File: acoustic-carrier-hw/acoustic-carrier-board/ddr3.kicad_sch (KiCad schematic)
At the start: 27 parts, among them IC1101 MT41K256M16TW-107_P

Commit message: [carrier] Added decoupling to LPDDR3 and routed VREF (next) finalize power supply
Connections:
- net VDDR_CORE renamed VLPDDR3_CORE
- net VDDR_DQ renamed VLPDDR3_DQ
- net VLPDRR3_V675 renamed VLPDDR3_V675
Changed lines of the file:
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@@
 	(wire
 		(pts
-			(xy 234.95 33.02) (xy 224.79 33.02)
+			(xy 237.49 33.02) (xy 224.79 33.02)
 		)
 		(stroke
@@
 	(wire
 		(pts
-			(xy 208.28 33.02) (xy 196.85 33.02)
+			(xy 212.09 33.02) (xy 196.85 33.02)
 		)
 		(stroke
@@
 		)
 	)
-	(label "VDDR_CORE"
-		(at 208.28 33.02 180)
-		(effects
-			(font
-				(size 1.27 1.27)
-			)
-			(justify right bottom)
-		)
-	)
 	(label "DDR3.LDM"
 		(at 180.34 82.55 180)
@@
 		)
 	)
+	(label "VLPDDR3_DQ"
+		(at 237.49 33.02 180)
+		(effects
+			(font
+				(size 1.27 1.27)
+			)
+			(justify right bottom)
+		)
+	)
 	(label "DDR3.CS#"
 		(at 261.62 93.98 0)
@@
 		)
 	)
-	(label "VDDR_DQ"
-		(at 57.15 99.06 0)
+	(label "VLPDDR3_DQ"
+		(at 43.18 99.06 0)
 		(effects
 			(font
@@
 		)
 	)
-	(label "VDDR_DQ"
-		(at 234.95 33.02 180)
-		(effects
-			(font
-				(size 1.27 1.27)
-			)
-			(justify right bottom)
-		)
-	)
 	(label "DDR3.DQ4"
 		(at 180.34 97.79 180)
@@
 		)
 	)
-	(label "VDDR_CORE"
+	(label "VLPDDR3_CORE"
 		(at 41.91 55.88 0)
 		(effects
@@
 			)
 			(justify left bottom)
+		)
+	)
+	(label "VLPDDR3_CORE"
+		(at 212.09 33.02 180)
+		(effects
+			(font
+				(size 1.27 1.27)
+			)
+			(justify right bottom)
 		)
 	)
@@
 		)
 	)
-	(global_label "VLPDRR3_V675"
+	(global_label "VLPDDR3_V675"
 		(shape passive)
 		(at 33.02 125.73 0)
@@
 		)
 	)
-	(global_label "VLPDRR3_V675"
+	(global_label "VLPDDR3_V675"
 		(shape passive)
 		(at 181.61 115.57 180)

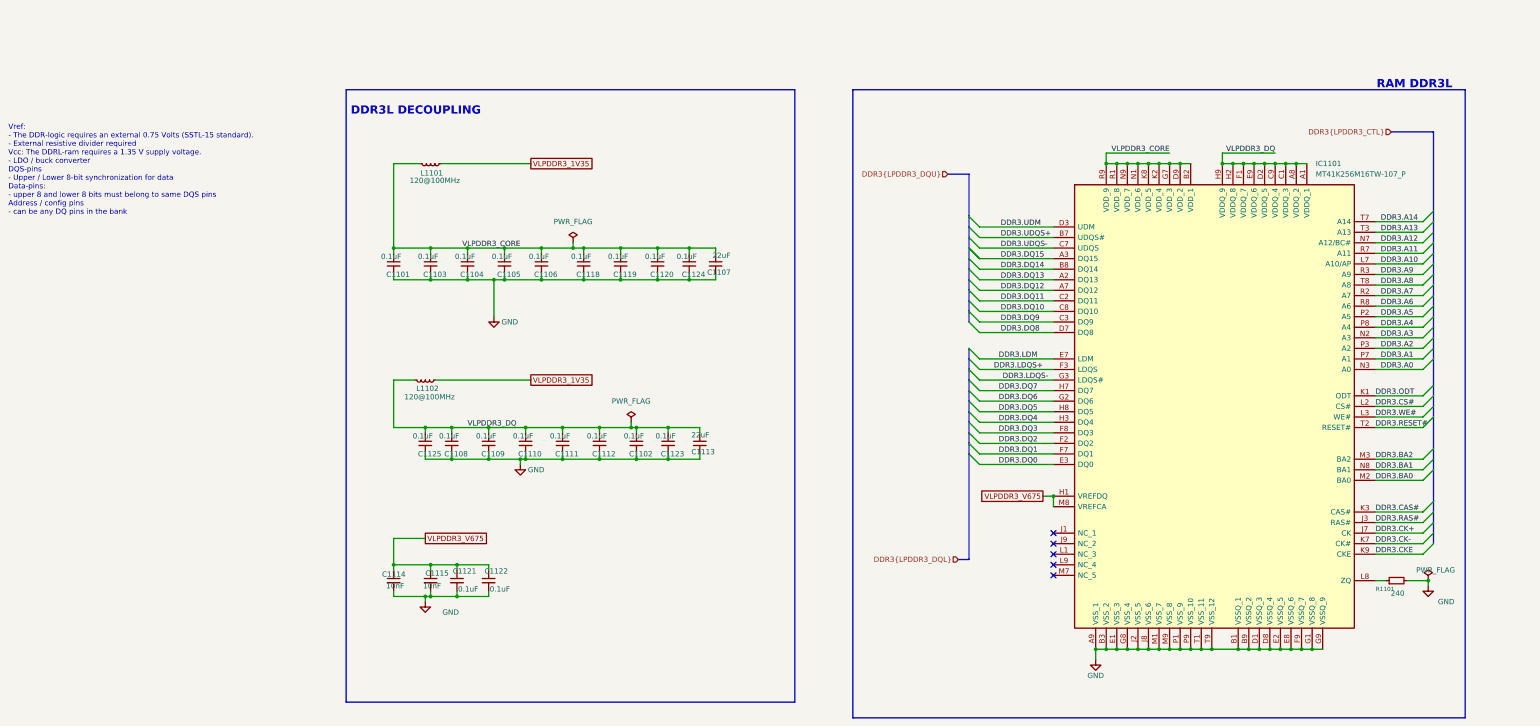
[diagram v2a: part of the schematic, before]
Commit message: [carrier] Further routing, ground plane removal underneath connectors, ..
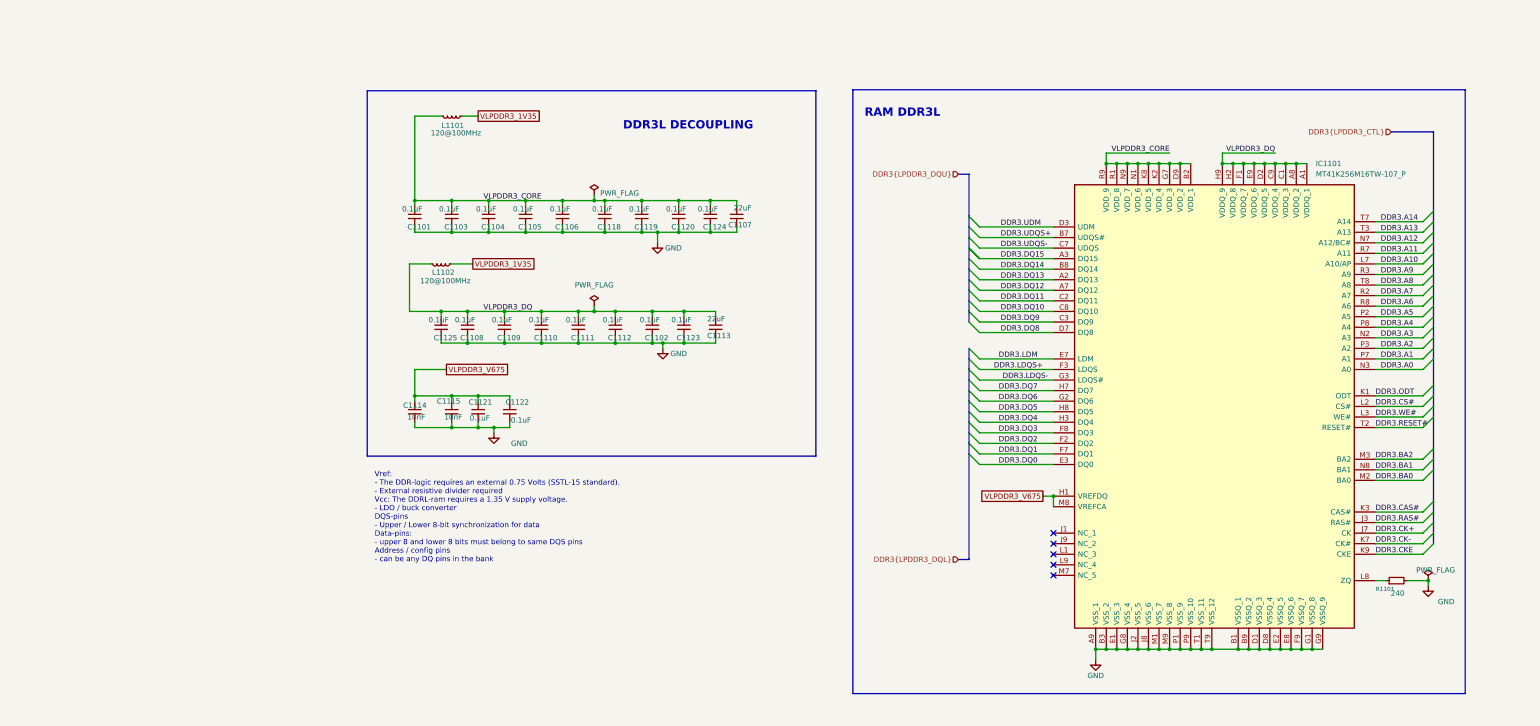
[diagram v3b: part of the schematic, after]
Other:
- moved on the sheet: C1101, C1102, C1103, C1104, C1105, C1106, C1107, C1108, C1109, C1110, C1111, C1112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

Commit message: [carrier] todo: recalculate validity window
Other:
- note added: "RAM LPDDR3"
- note removed: "RAM DDR3L"
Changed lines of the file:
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@@
 		)
 	)
-	(text "RAM DDR3L"
+	(text "RAM LPDDR3"
 		(exclude_from_sim no)
 		(at 147.828 23.368 0)

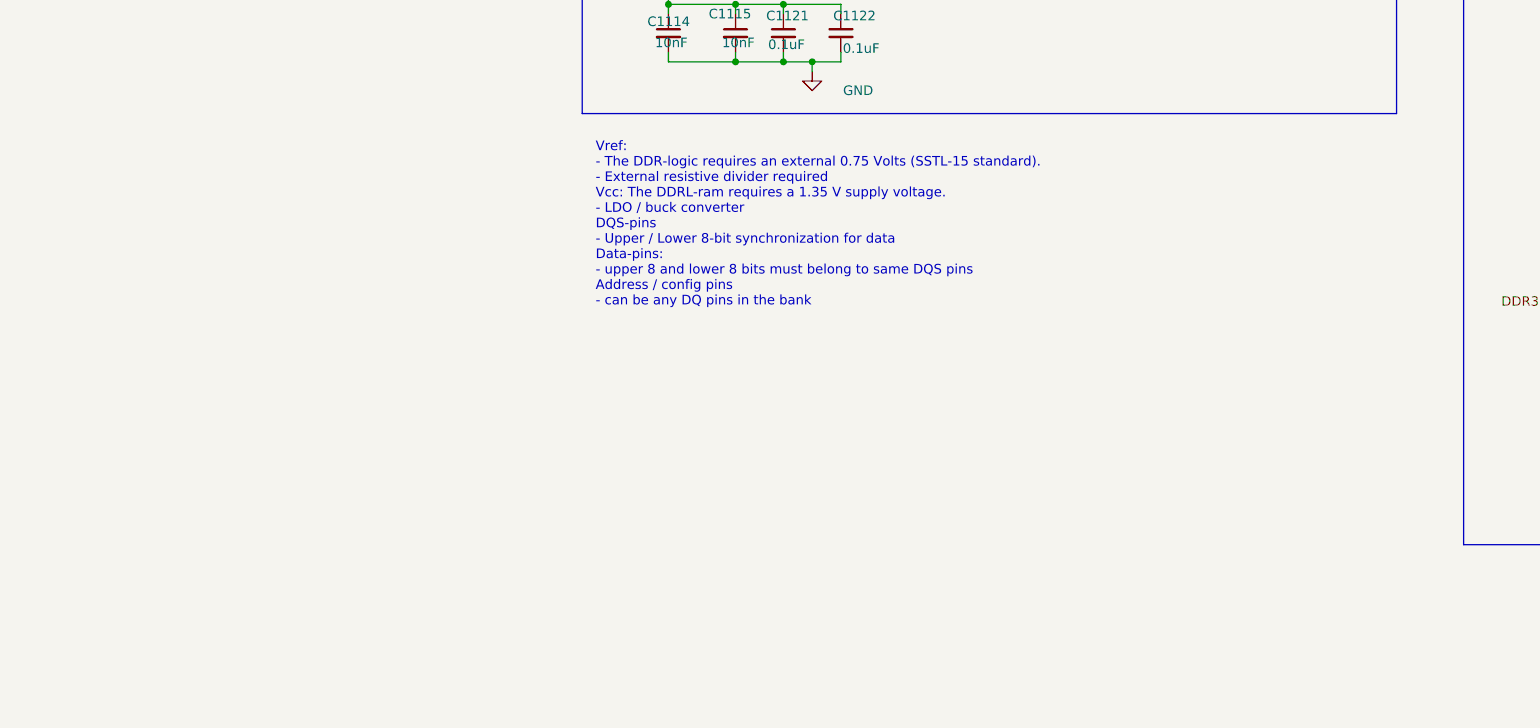
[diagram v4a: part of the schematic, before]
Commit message: [carrier] Added testpoints to lpddr3 (next) do final checks before ordering
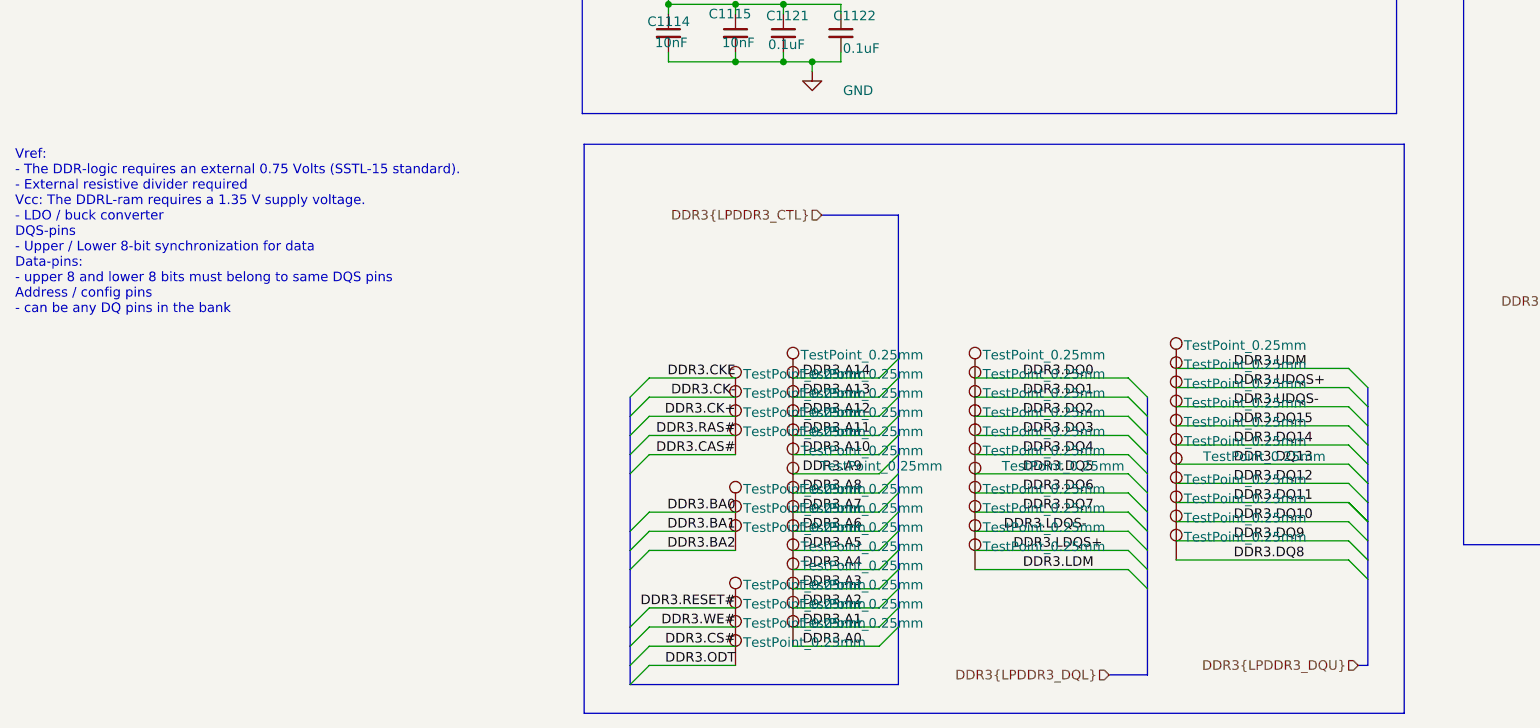
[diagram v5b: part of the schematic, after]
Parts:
- added TP1101, TP1102, TP1103, TP1104, TP1105, TP1106, TP1107, TP1108, TP1109, TP1110, TP1111, TP1112, TP1113, TP1114, TP1115, TP1116, TP1117, TP1118, TP1119, TP1120, TP1121, TP1122, TP1123, TP1124, TP1125, TP1126, TP1127, TP1128, TP1129, TP1130, TP1131, TP1132, TP1133, TP1134, TP1135, TP1136, TP1137, TP1138, TP1139, TP1140, TP1141, TP1142, TP1143, TP1144, TP1145, TP1146, TP1147, TP1148: TestPoint_0.25mm, iw-misc:TestPoint_Pad_D0.25mm, symbol iw-misc:TestPoint_0.25mm
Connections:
- net DDR3.A0: now also TP1137.1
- net DDR3.A1: now also TP1136.1
- net DDR3.A10: now also TP1127.1
- net DDR3.A11: now also TP1126.1
- net DDR3.A12: now also TP1125.1
- net DDR3.A13: now also TP1102.1
- net DDR3.A14: now also TP1101.1
- net DDR3.A2: now also TP1135.1
- net DDR3.A3: now also TP1134.1
- net DDR3.A4: now also TP1133.1
- net DDR3.A5: now also TP1132.1
- net DDR3.A6: now also TP1131.1
- net DDR3.A7: now also TP1130.1
- net DDR3.A8: now also TP1129.1
- net DDR3.A9: now also TP1128.1
- net DDR3.BA0: now also TP1146.1
- net DDR3.BA1: now also TP1147.1
- net DDR3.BA2: now also TP1148.1
- net DDR3.CAS#: now also TP1145.1
- net DDR3.CK+: now also TP1143.1
- net DDR3.CK-: now also TP1142.1
- net DDR3.CS#: now also TP1140.1
- net DDR3.DQ0: now also TP1103.1
- net DDR3.DQ1: now also TP1106.1
- net DDR3.DQ10: now also TP1112.1
- net DDR3.DQ11: now also TP1111.1
- net DDR3.DQ12: now also TP1110.1
- net DDR3.DQ13: now also TP1115.1
- net DDR3.DQ14: now also TP1109.1
- net DDR3.DQ15: now also TP1108.1
- net DDR3.DQ2: now also TP1116.1
- net DDR3.DQ3: now also TP1117.1
- net DDR3.DQ4: now also TP1118.1
- net DDR3.DQ5: now also TP1119.1
- net DDR3.DQ6: now also TP1120.1
- net DDR3.DQ7: now also TP1121.1
- net DDR3.DQ8: now also TP1114.1
- net DDR3.DQ9: now also TP1113.1
- net DDR3.LDM: now also TP1124.1
- net DDR3.LDQS+: now also TP1123.1
- net DDR3.LDQS-: now also TP1122.1
- net DDR3.ODT: now also TP1141.1
- net DDR3.RAS#: now also TP1144.1
- net DDR3.RESET#: now also TP1138.1
- net DDR3.UDM: now also TP1104.1
- net DDR3.UDQS+: now also TP1105.1
- net DDR3.UDQS-: now also TP1107.1
- net DDR3.WE#: now also TP1139.1

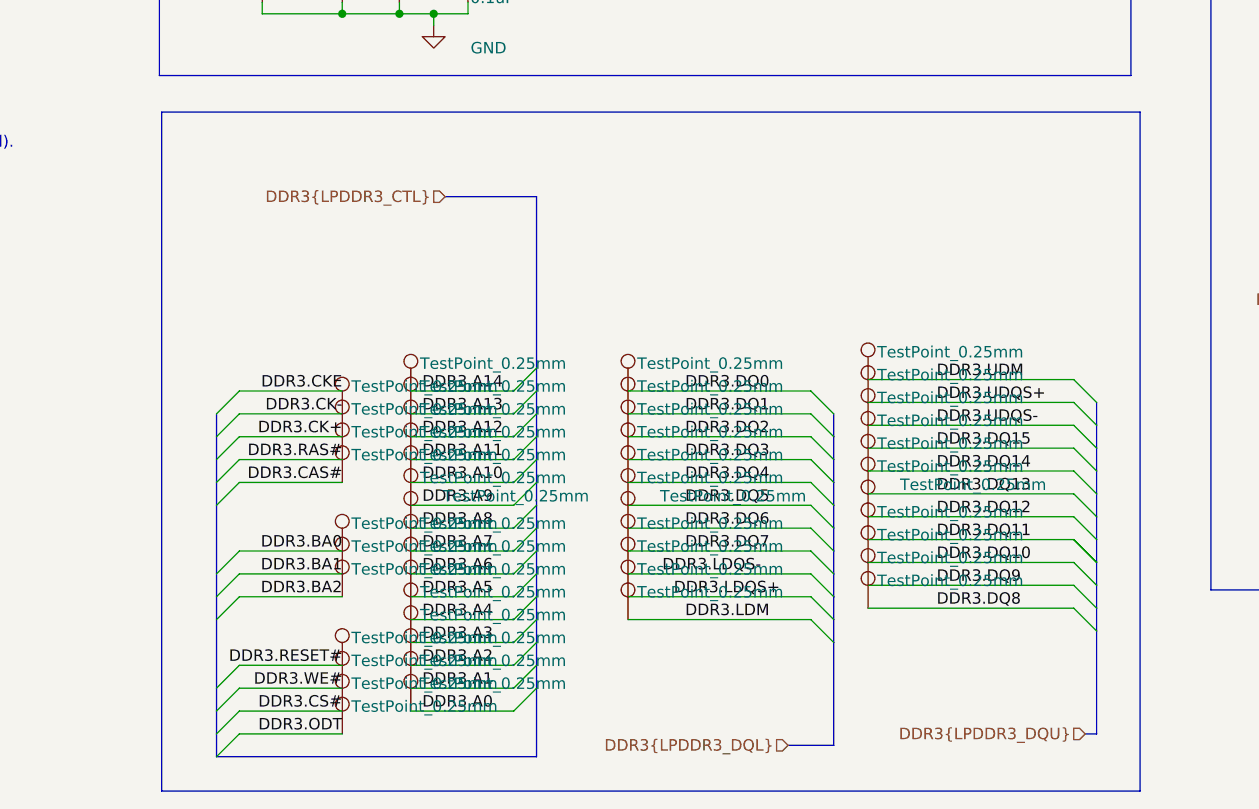
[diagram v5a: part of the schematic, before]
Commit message: [carrier] finished for production (next) reroute the LPDDR3, with appropriate CMD-CTRL bus delays, and change banks for command-control
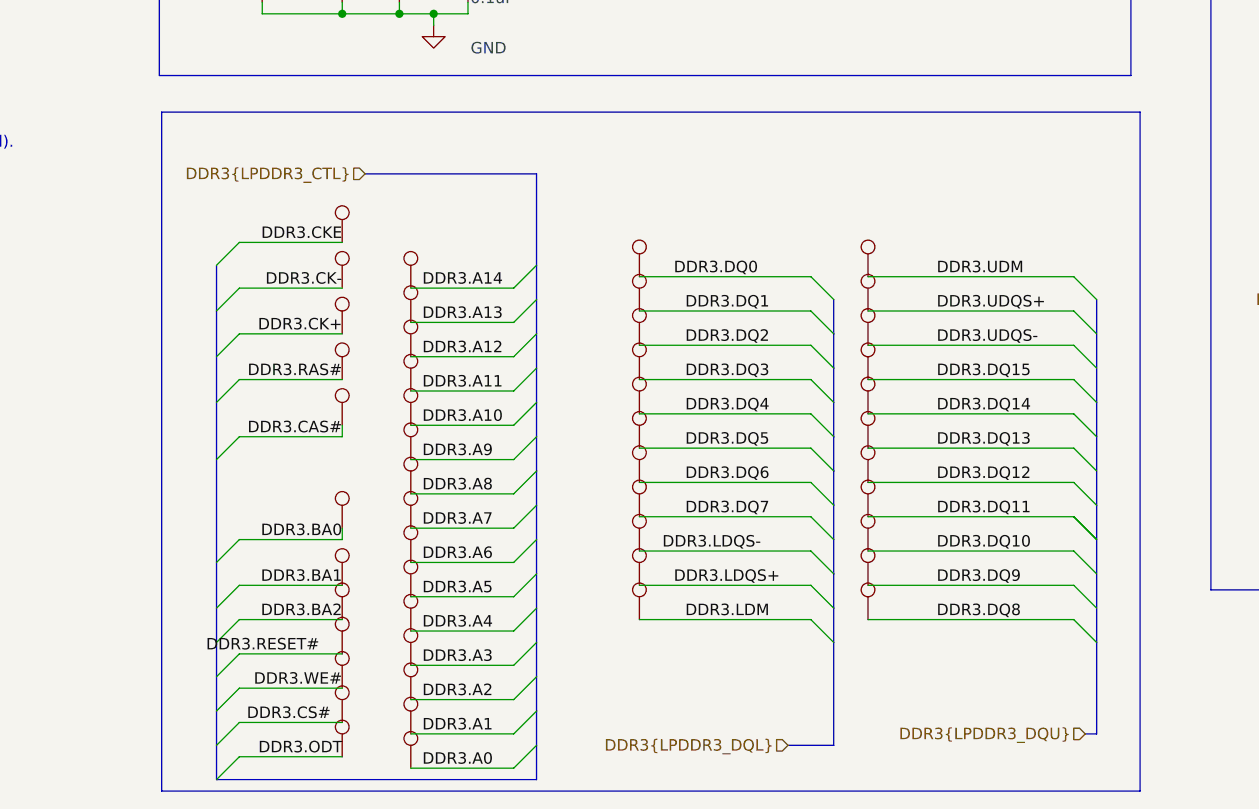
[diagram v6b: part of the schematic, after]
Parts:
- added TP1149: TestPoint_0.25mm, iw-misc:TestPoint_Pad_D0.25mm, symbol iw-misc:TestPoint_0.25mm
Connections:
- net DDR3.CKE: now also TP1149.1

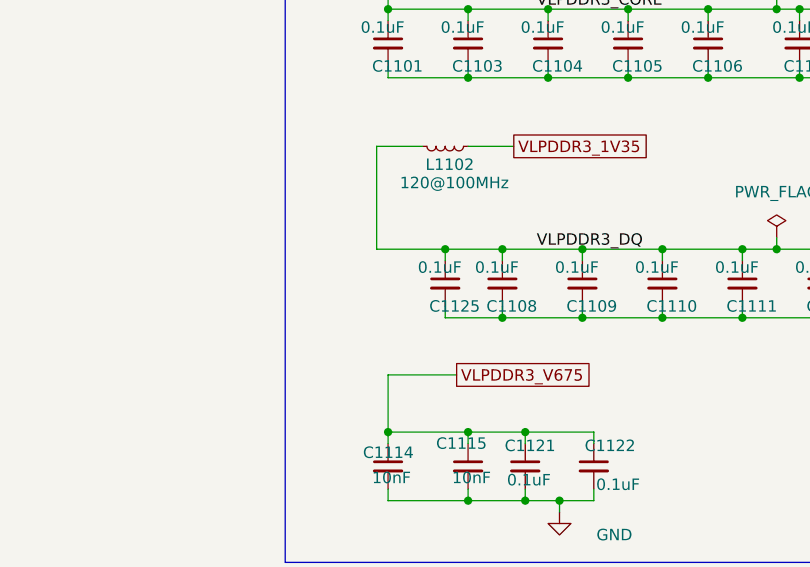
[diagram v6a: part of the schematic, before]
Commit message: [carrier] Finished routing, layed out lpddr3 capacitors (next) route power on plane
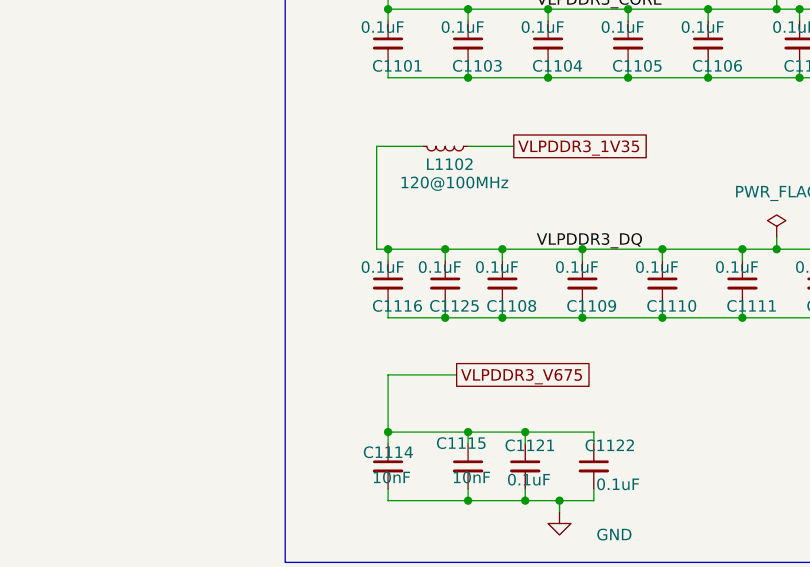
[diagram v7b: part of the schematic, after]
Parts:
- added C1116: 0.1uF, Capacitor_SMD:C_0201_0603Metric, symbol Device:C_Small
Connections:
- net GND: now also C1116.2
- net VLPDDR3_DQ: now also C1116.1
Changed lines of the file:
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@@
 	)
 	(junction
+		(at 36.83 78.74)
+		(diameter 0)
+		(color 0 0 0 0)
+	)
+	(junction
 		(at 238.76 152.4)
 		(diameter 0)
@@
 	)
 	(junction
+		(at 30.48 71.12)
+		(diameter 0)
+		(color 0 0 0 0)
+	)
+	(junction
 		(at 57.15 52.07)
 		(diameter 0)
@@
 	(wire
 		(pts
+			(xy 30.48 71.12) (xy 36.83 71.12)
+		)
+		(stroke
+			(width 0)
+			(type default)
+		)
+	)
+	(wire
+		(pts
 			(xy 184.15 68.58) (xy 166.37 68.58)
 		)
@@
 	(wire
 		(pts
+			(xy 30.48 77.47) (xy 30.48 78.74)
+		)
+		(stroke
+			(width 0)
+			(type default)
+		)
+	)
+	(wire
+		(pts
 			(xy 34.29 59.69) (xy 29.21 59.69)
 		)
@@
 	(wire
 		(pts
+			(xy 30.48 78.74) (xy 36.83 78.74)
+		)
+		(stroke
+			(width 0)
+			(type default)
+		)
+	)
+	(wire
+		(pts
 			(xy 101.6 44.45) (xy 93.98 44.45)
 		)
@@
 	(wire
 		(pts
-			(xy 29.21 71.12) (xy 36.83 71.12)
+			(xy 29.21 71.12) (xy 30.48 71.12)
 		)
 		(stroke
@@
 	(wire
 		(pts
+			(xy 30.48 72.39) (xy 30.48 71.12)
+		)
+		(stroke
+			(width 0)
+			(type default)
+		)
+	)
+	(wire
+		(pts
 			(xy 261.62 135.89) (xy 264.16 135.89)
 		)
@@
 					(unit 1)
 				)
+			)
+		)
+	)
+	(symbol
+		(lib_id "Device:C_Small")
+		(at 30.48 74.93 0)
+		(unit 1)
+		(exclude_from_sim no)
+		(in_bom yes)
+		(on_board yes)
+		(dnp no)
+		(property "Reference" "C1116"
+			(at 28.702 77.47 0)
+			(effects
+				(font
+					(size 1.27 1.27)
+				)
+				(justify left)
+			)
+		)
+		(property "Value" "0.1uF"
+			(at 27.432 73.152 0)
+			(effects
+				(font
+					(size 1.27 1.27)
+				)
+				(justify left)
+			)
+		)
+		(property "Footprint" "Capacitor_SMD:C_0201_0603Metric"
+			(at 30.48 74.93 0)
+			(effects
+				(font
+					(size 1.27 1.27)
+				)
+				(hide yes)
+			)
+		)
+		(property "Datasheet" "https://jlcpcb.com/api/file/downloadByFileSystemAccessId/8603345729432014848"
+			(at 30.48 74.93 0)
+			(effects
+				(font
+					(size 1.27 1.27)
+				)
+				(hide yes)
+			)
+		)
+		(property "Description" "X7R, +-10%"
+			(at 30.48 74.93 0)
+			(effects
+				(font
+					(size 1.27 1.27)
+				)
+				(hide yes)
+			)
+		)
+		(property "LPN" "C22435929"
+			(at 30.48 74.93 0)
+			(effects
+				(font
+					(size 1.27 1.27)
+				)
+				(hide yes)
+			)
+		)
+		(property "MPN" "CGA0201X7R104K160ET "
+			(at 30.48 74.93 0)
+			(effects
+				(font
+					(size 1.27 1.27)
+				)
+				(hide yes)
+			)
+		)
+		(property "Availability" ""
+			(at 30.48 74.93 0)
+			(effects
+				(font
+					(size 1.27 1.27)
+				)
+				(hide yes)
+			)
+		)
+		(property "Check_prices" ""
+			(at 30.48 74.93 0)
+			(effects
+				(font
+					(size 1.27 1.27)
+				)
+				(hide yes)
+			)
+		)
+		(pin "2"
+		)
+		(pin "1"
+		)
+		(instances
+			(project "acoustic-carrier-board"
+				(path "/25b015c9-ab13-4427-b72c-b6f348597100/f2b9f5c5-2b83-49a1-9584-962bb926f77f"
+					(reference "C1116")
+					(unit 1)
+				)
